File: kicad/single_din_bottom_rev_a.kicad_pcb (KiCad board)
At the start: 2 copper layers, 86 x 14 mm, 9 parts, among them J1 Conn_01x04, J2 Conn_01x04, J3 Conn_01x04, J4 Conn_01x04, U1 R-78B3.3-1.0 (Recom)

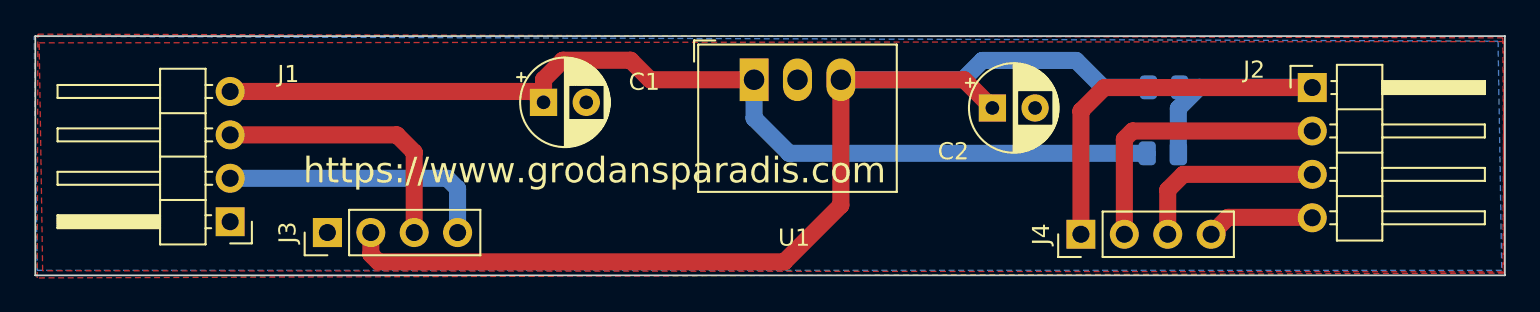
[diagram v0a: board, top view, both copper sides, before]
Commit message: Added measurements to drawing
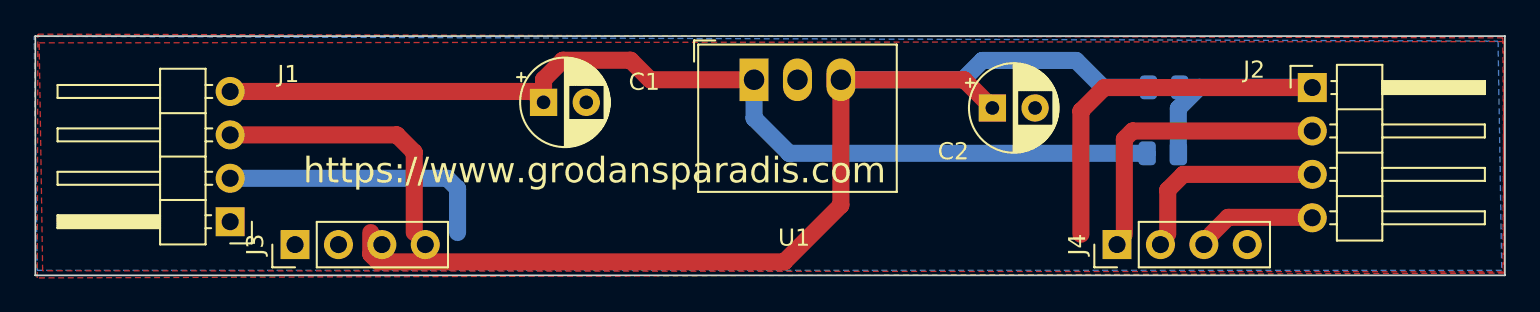
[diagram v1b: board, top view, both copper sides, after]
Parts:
- moved J4 2.20 mm to (93.3, 178.2)
- moved J3 2.02 mm to (45.2, 178.2)
